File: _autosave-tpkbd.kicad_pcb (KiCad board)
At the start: 2 copper layers, 43 x 38 mm, 21 parts, among them CON1 AVR-ISP-6, J1 CONN_01X02, J2 CONN_01X01, J3 USB_OTG, J4 CONN_02X20, J5 CONN_01X04, J6 GS2, J7 0, U1 ATMEGA8515-16AU, U2 AP111733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

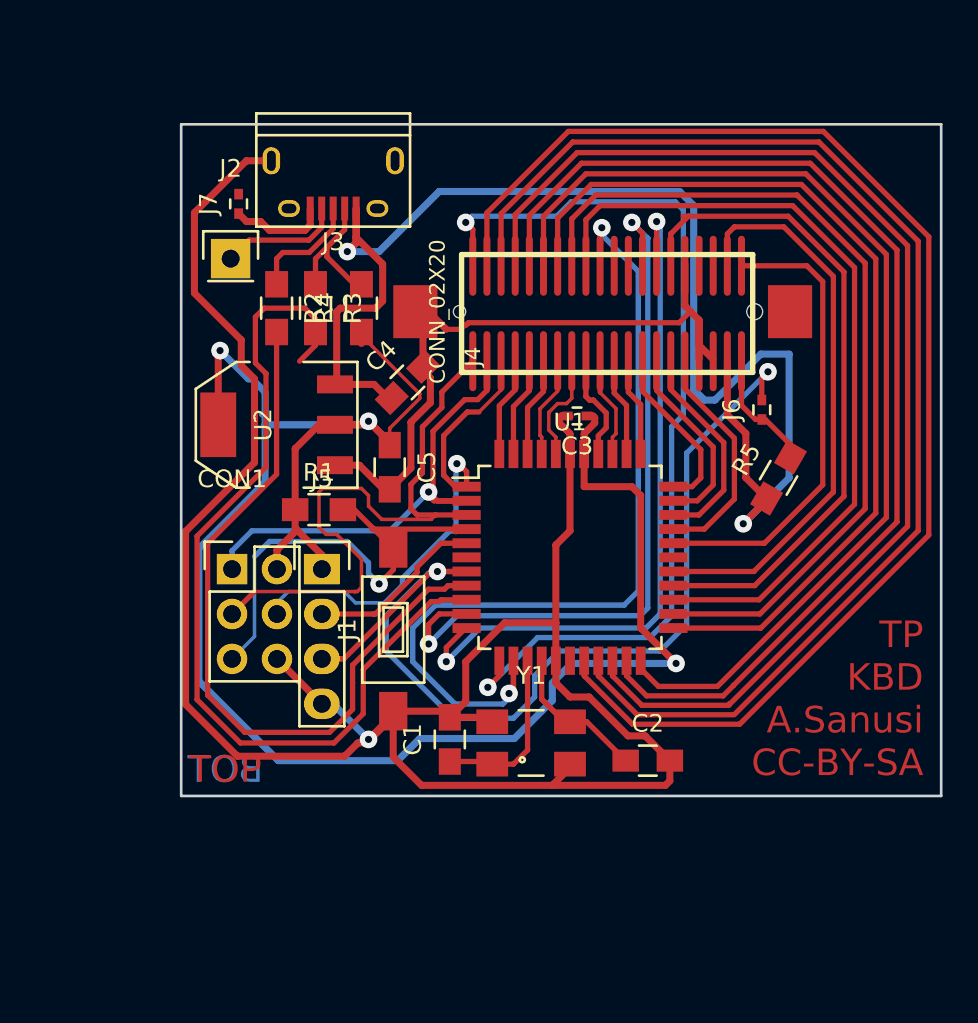
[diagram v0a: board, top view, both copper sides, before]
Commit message: added a LED
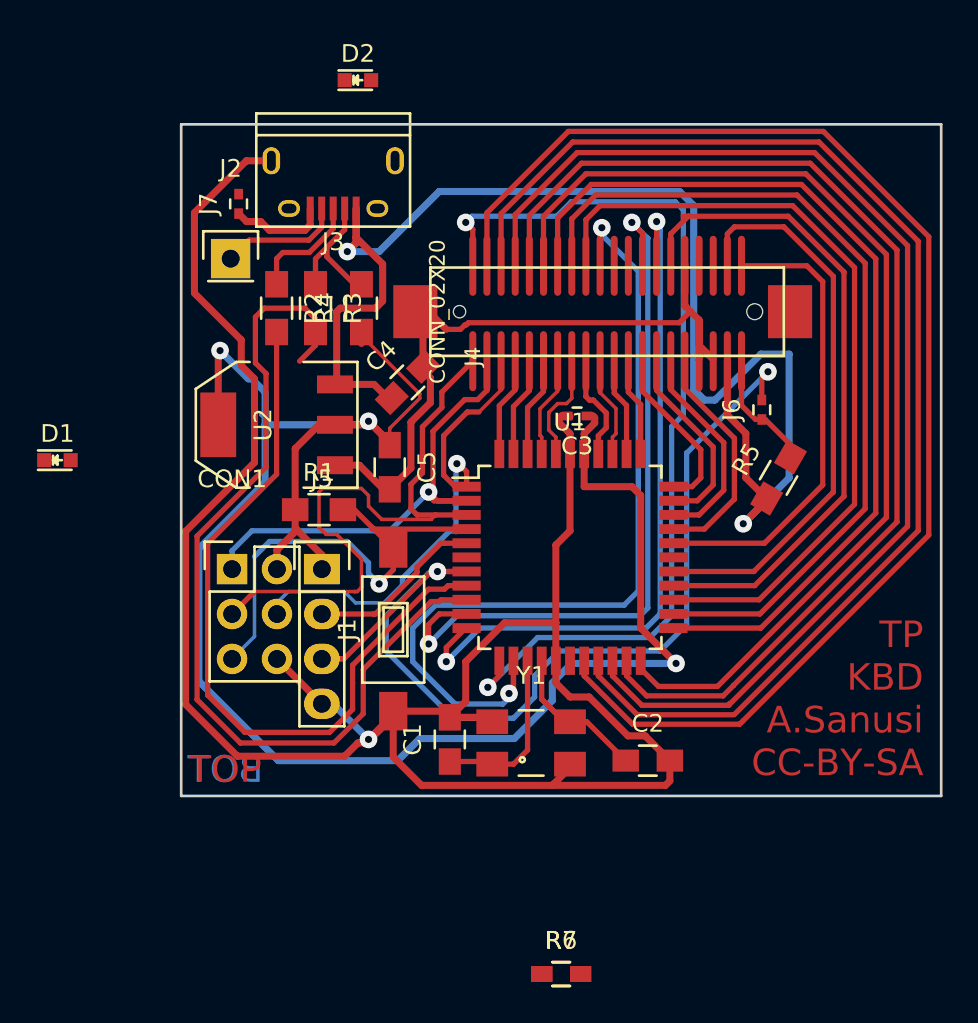
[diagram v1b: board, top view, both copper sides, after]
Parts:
- added D1: LED, LEDs:LED-0603, F.Cu at (46.0, 44.0)
- added D2: LED, LEDs:LED-0603, F.Cu at (63.0, 22.5)
- added R6, R7: R, Resistors_SMD:R_0603_HandSoldering, F.Cu at (74.5, 73.1)
- J4: footprint KX14:KX14 -> KX14
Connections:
- J4 pad 41: GND -> (no net)
- U1 pad 10: /kb_id0 -> /led
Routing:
- net /led: track 0.00 -> 5.76 mm, vias 0 -> 1
- net /kb_id0: track 41.7 -> 35.9 mm, vias 2 -> 1
